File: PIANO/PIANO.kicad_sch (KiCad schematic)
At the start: 32 parts, among them J1 Conn_01x02_Male, SW1 ON/OFF, SW2 RESET, U1 LF33_TO220, U2 ESP32-S2-SOLO, U3 Opamp_Dual, U4 Opamp_Dual

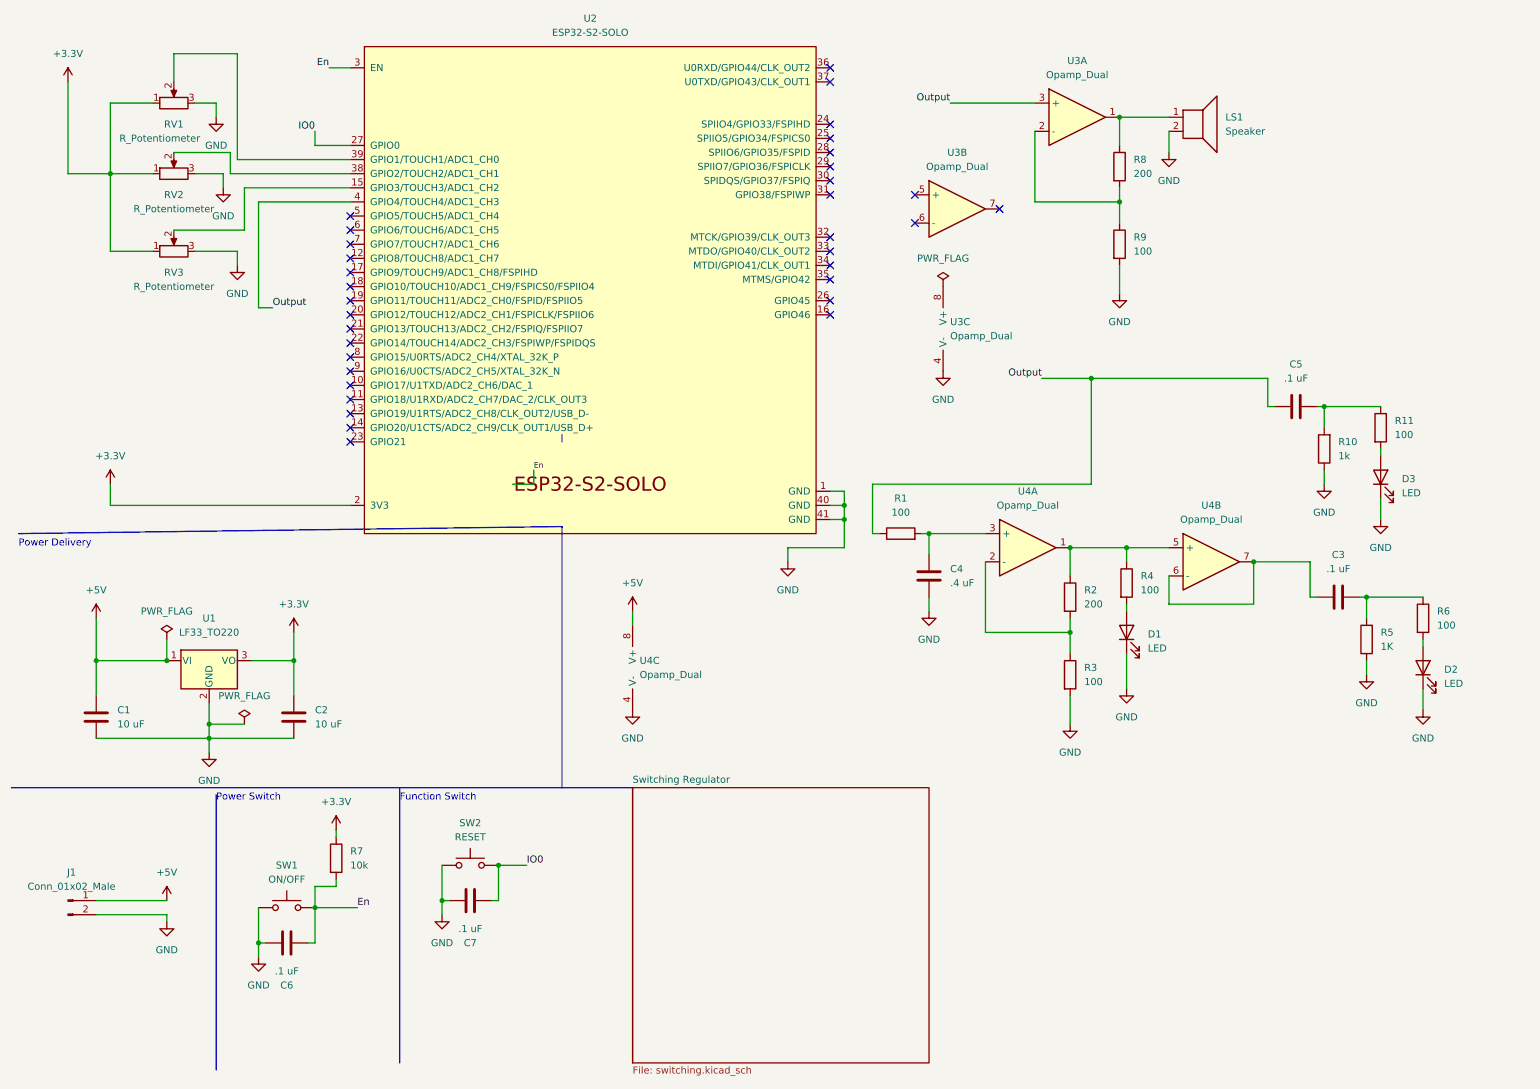
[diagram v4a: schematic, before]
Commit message: added usb component
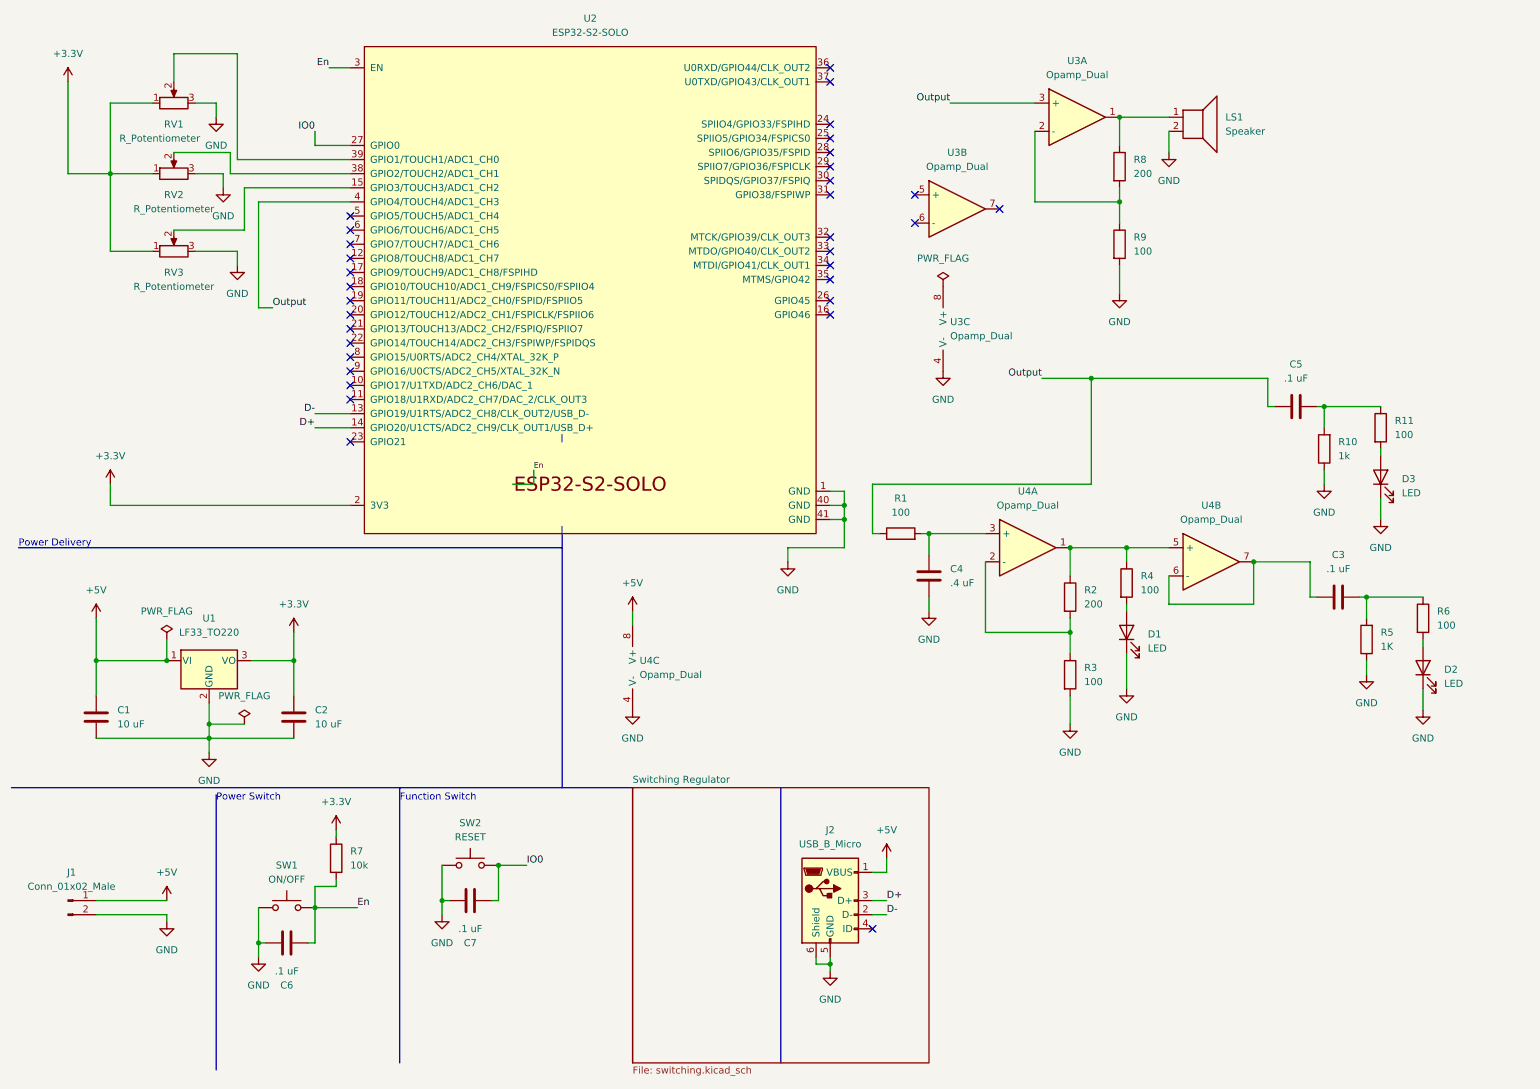
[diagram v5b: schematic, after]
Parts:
- added J2: USB_B_Micro, Connector_USB:USB_Micro-B_GCT_USB3076-30-A, symbol Connector:USB_B_Micro
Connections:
- net +5V: now also J2.1 (VBUS)
- net GND: now also J2.5 (GND), J2.6 (Shield)
- net D-: now reaches U2.13 (GPIO19/U1RTS/ADC2_CH8/CLK_OUT2/USB_D-)
- net D-: now also J2.2 (D-)
- net D+: now reaches U2.14 (GPIO20/U1CTS/ADC2_CH9/CLK_OUT1/USB_D+)
- net D+: now also J2.3 (D+)
- no-connect marks 34 -> 33
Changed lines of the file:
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@@
   (junction (at 88.9 168.91) (diameter 0) (color 0 0 0 0)
   )
+  (junction (at 158.75 180.34) (diameter 0) (color 0 0 0 0)
+  )
   (junction (at 212.09 105.41) (diameter 0) (color 0 0 0 0)
   )
@@
   (junction (at 161.29 97.79) (diameter 0) (color 0 0 0 0)
   )
+  (no_connect (at 166.37 173.99))
   (no_connect (at 189.23 44.45))
   (no_connect (at 173.99 41.91))
@@
   (no_connect (at 72.39 50.8))
   (no_connect (at 72.39 78.74))
-  (no_connect (at 72.39 81.28))
-  (no_connect (at 72.39 83.82))
   (no_connect (at 72.39 53.34))
   (no_connect (at 72.39 55.88))
@@
     (stroke (width 0) (type default) (color 0 0 0 0))
   )
+  (wire (pts (xy 156.21 179.07) (xy 156.21 180.34))
+    (stroke (width 0) (type default) (color 0 0 0 0))
+  )
   (wire (pts (xy 212.09 124.46) (xy 212.09 130.81))
     (stroke (width 0) (type default) (color 0 0 0 0))
@@
     (stroke (width 0) (type default) (color 0 0 0 0))
   )
+  (wire (pts (xy 166.37 168.91) (xy 168.91 168.91))
+    (stroke (width 0) (type default) (color 0 0 0 0))
+  )
   (wire (pts (xy 219.71 115.57) (xy 219.71 110.49))
     (stroke (width 0) (type default) (color 0 0 0 0))
@@
     (stroke (width 0) (type default) (color 0 0 0 0))
   )
+  (wire (pts (xy 158.75 180.34) (xy 158.75 181.61))
+    (stroke (width 0) (type default) (color 0 0 0 0))
+  )
   (wire (pts (xy 176.53 114.3) (xy 176.53 116.84))
     (stroke (width 0) (type default) (color 0 0 0 0))
@@
     (stroke (width 0) (type default) (color 0 0 0 0))
   )
+  (wire (pts (xy 166.37 171.45) (xy 168.91 171.45))
+    (stroke (width 0) (type default) (color 0 0 0 0))
+  )
   (wire (pts (xy 245.11 107.95) (xy 245.11 114.3))
     (stroke (width 0) (type default) (color 0 0 0 0))
@@
     (stroke (width 0) (type default) (color 0 0 0 0))
   )
+  (wire (pts (xy 66.04 81.28) (xy 72.39 81.28))
+    (stroke (width 0) (type default) (color 0 0 0 0))
+  )
   (polyline (pts (xy 48.26 149.86) (xy 48.26 199.39))
     (stroke (width 0) (type default) (color 0 0 0 0))
@@
     (stroke (width 0) (type default) (color 0 0 0 0))
   )
+  (polyline (pts (xy 12.7 105.41) (xy 110.49 105.41))
+    (stroke (width 0) (type default) (color 0 0 0 0))
+  )
   (wire (pts (xy 255.27 114.3) (xy 255.27 118.11))
     (stroke (width 0) (type default) (color 0 0 0 0))
@@
     (stroke (width 0) (type default) (color 0 0 0 0))
   )
+  (wire (pts (xy 156.21 180.34) (xy 158.75 180.34))
+    (stroke (width 0) (type default) (color 0 0 0 0))
+  )
   (wire (pts (xy 180.34 25.4) (xy 195.58 25.4))
     (stroke (width 0) (type default) (color 0 0 0 0))
@@
     (stroke (width 0) (type default) (color 0 0 0 0))
   )
+  (wire (pts (xy 166.37 163.83) (xy 168.91 163.83))
+    (stroke (width 0) (type default) (color 0 0 0 0))
+  )
   (wire (pts (xy 257.81 87.63) (xy 257.81 88.9))
     (stroke (width 0) (type default) (color 0 0 0 0))
@@
     (stroke (width 0) (type default) (color 0 0 0 0))
   )
+  (wire (pts (xy 158.75 179.07) (xy 158.75 180.34))
+    (stroke (width 0) (type default) (color 0 0 0 0))
+  )
   (wire (pts (xy 55.88 43.18) (xy 72.39 43.18))
     (stroke (width 0) (type default) (color 0 0 0 0))
@@
     (stroke (width 0) (type default) (color 0 0 0 0))
   )
-  (polyline (pts (xy 12.7 102.87) (xy 110.49 101.6))
+  (polyline (pts (xy 149.86 148.59) (xy 149.86 198.12))
     (stroke (width 0) (type default) (color 0 0 0 0))
   )
@@
     (stroke (width 0) (type default) (color 0 0 0 0))
   )
+  (wire (pts (xy 72.39 83.82) (xy 66.04 83.82))
+    (stroke (width 0) (type default) (color 0 0 0 0))
+  )
   (wire (pts (xy 39.37 121.92) (xy 39.37 125.73))
     (stroke (width 0) (type default) (color 0 0 0 0))
   )
   (wire (pts (xy 88.9 168.91) (xy 90.17 168.91))
+    (stroke (width 0) (type default) (color 0 0 0 0))
+  )
+  (wire (pts (xy 168.91 161.29) (xy 168.91 163.83))
     (stroke (width 0) (type default) (color 0 0 0 0))
   )
@@
     (effects (font (size 1.27 1.27)) (justify left bottom))
   )
+  (label "D+" (at 168.91 168.91 0)
+    (effects (font (size 1.27 1.27)) (justify left bottom))
+  )
   (label "Output" (at 180.34 25.4 180)
     (effects (font (size 1.27 1.27)) (justify right bottom))
   )
+  (label "D-" (at 168.91 171.45 0)
+    (effects (font (size 1.27 1.27)) (justify left bottom))
+  )
   (label "IO0" (at 104.14 162.56 0)
     (effects (font (size 1.27 1.27)) (justify left bottom))
@@
     (effects (font (size 1.27 1.27)) (justify left bottom))
   )
+  (label "D-" (at 66.04 81.28 180)
+    (effects (font (size 1.27 1.27)) (justify right bottom))
+  )
   (label "IO0" (at 66.04 30.48 180)
     (effects (font (size 1.27 1.27)) (justify right bottom))
@@
     (effects (font (size 1.27 1.27)) (justify right bottom))
   )
+  (label "D+" (at 66.04 83.82 180)
+    (effects (font (size 1.27 1.27)) (justify right bottom))
+  )
   (symbol (lib_id "power:GND") (at 212.09 130.81 0) (unit 1)
     (in_bom yes) (on_board yes) (fields_autoplaced)
@@
     )
     (pin "1")
+  )
+  (symbol (lib_id "Connector:USB_B_Micro") (at 158.75 168.91 0) (unit 1)
+    (in_bom yes) (on_board yes) (fields_autoplaced)
+    (property "Reference" "J2" (id 0) (at 158.75 156.21 0))
+    (property "Value" "USB_B_Micro" (id 1) (at 158.75 158.75 0))
+    (property "Footprint" "Connector_USB:USB_Micro-B_GCT_USB3076-30-A" (id 2) (at 162.56 170.18 0)
+      (effects (font (size 1.27 1.27)) hide)
+    )
+    (property "Datasheet" "~" (id 3) (at 162.56 170.18 0)
+      (effects (font (size 1.27 1.27)) hide)
+    )
+    (pin "1")
+    (pin "2")
+    (pin "3")
+    (pin "4")
+    (pin "5")
+    (pin "6")
   )
   (symbol (lib_id "power:GND") (at 247.65 93.98 0) (unit 1)
@@
     (pin "1")
   )
+  (symbol (lib_id "power:GND") (at 158.75 181.61 0) (unit 1)
+    (in_bom yes) (on_board yes) (fields_autoplaced)
+    (property "Reference" "#PWR0120" (id 0) (at 158.75 187.96 0)
+      (effects (font (size 1.27 1.27)) hide)
+    )
+    (property "Value" "GND" (id 1) (at 158.75 186.69 0))
+    (property "Footprint" "" (id 2) (at 158.75 181.61 0)
+      (effects (font (size 1.27 1.27)) hide)
+    )
+    (property "Datasheet" "" (id 3) (at 158.75 181.61 0)
+      (effects (font (size 1.27 1.27)) hide)
+    )
+    (pin "1")
+  )
+  (symbol (lib_id "power:+5V") (at 168.91 161.29 0) (unit 1)
+    (in_bom yes) (on_board yes) (fields_autoplaced)
+    (property "Reference" "#PWR0131" (id 0) (at 168.91 165.1 0)
+      (effects (font (size 1.27 1.27)) hide)
+    )
+    (property "Value" "+5V" (id 1) (at 168.91 156.21 0))
+    (property "Footprint" "" (id 2) (at 168.91 161.29 0)
+      (effects (font (size 1.27 1.27)) hide)
+    )
+    (property "Datasheet" "" (id 3) (at 168.91 161.29 0)
+      (effects (font (size 1.27 1.27)) hide)
+    )
+    (pin "1")
+  )
   (symbol (lib_id "Device:Opamp_Dual") (at 227.33 107.95 0) (unit 2)
     (in_bom yes) (on_board yes) (fields_autoplaced)
@@
       (reference "#PWR0119") (unit 1) (value "GND") (footprint "")
     )
+    (path "/b3b28669-632c-4c80-a60b-e834452f83f8"
+      (reference "#PWR0120") (unit 1) (value "GND") (footprint "")
+    )
     (path "/742a9aab-a67a-425b-97b2-92ae80069c02"
       (reference "#PWR0121") (unit 1) (value "GND") (footprint "")
@@
       (reference "#PWR0130") (unit 1) (value "GND") (footprint "")
     )
+    (path "/b7e13384-6069-4824-aa39-b221e5fe7ed9"
+      (reference "#PWR0131") (unit 1) (value "+5V") (footprint "")
+    )
     (path "/7f576ece-c9bc-4f26-b53f-08232bf521db/f0b7f140-6667-44f5-a73a-11f6423c8f34"
       (reference "#PWR0133") (unit 1) (value "GND") (footprint "")
@@
       (reference "J1") (unit 1) (value "Conn_01x02_Male") (footprint "Connector_PinHeader_2.54mm:PinHeader_1x02_P2.54mm_Vertical")
     )
+    (path "/0ccf3bde-866e-4231-b785-fc8e0833134f"
+      (reference "J2") (unit 1) (value "USB_B_Micro") (footprint "Connector_USB:USB_Micro-B_GCT_USB3076-30-A")
+    )
     (path "/7f576ece-c9bc-4f26-b53f-08232bf521db/5376daf9-540f-428d-a080-08d7704055f2"
